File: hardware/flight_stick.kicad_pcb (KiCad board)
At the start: 4 copper layers, 76 x 51.5 mm, 60 parts, among them J1 Conn_01x04_Male, J10 USB_C_Receptacle_USB2.0, J12 Load Cell 2, J2 Conn_02x05_Odd_Even, J3 Conn_01x04_Male, J4 Load Cell 3, J6 Load Cell 1, J9 Conn_ST_STDC14, SW1 KMR223G LFG, U1 TPS62175DQC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

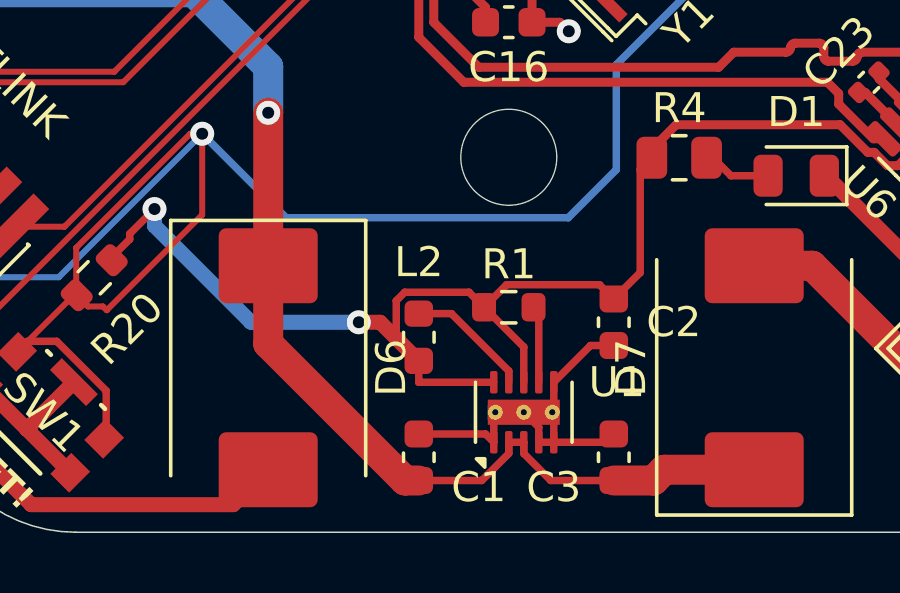
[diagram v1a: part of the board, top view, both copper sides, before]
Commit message: tied PG to mcu reset
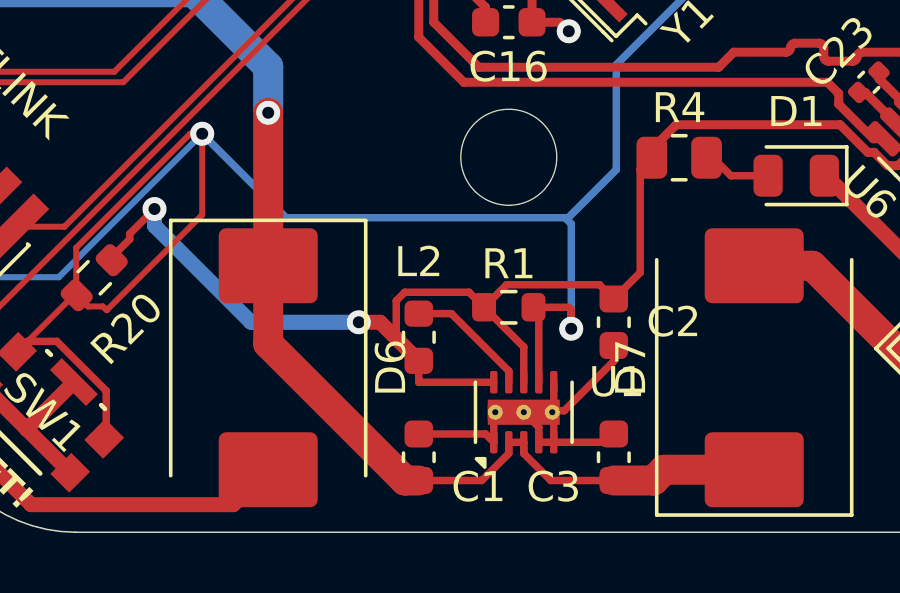
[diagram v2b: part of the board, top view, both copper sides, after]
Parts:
- R1: value 100k -> 10k
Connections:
- R1 pad 2: /Power/PG -> /RESET
- U1 pad 7: /Power/PG -> /RESET
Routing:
- net /RESET: track 64.8 -> 72.9 mm, vias 3 -> 4
- net /Power/PG: track 2.32 -> 0.00 mm
- net GND: track 155.9 -> 156.6 mm

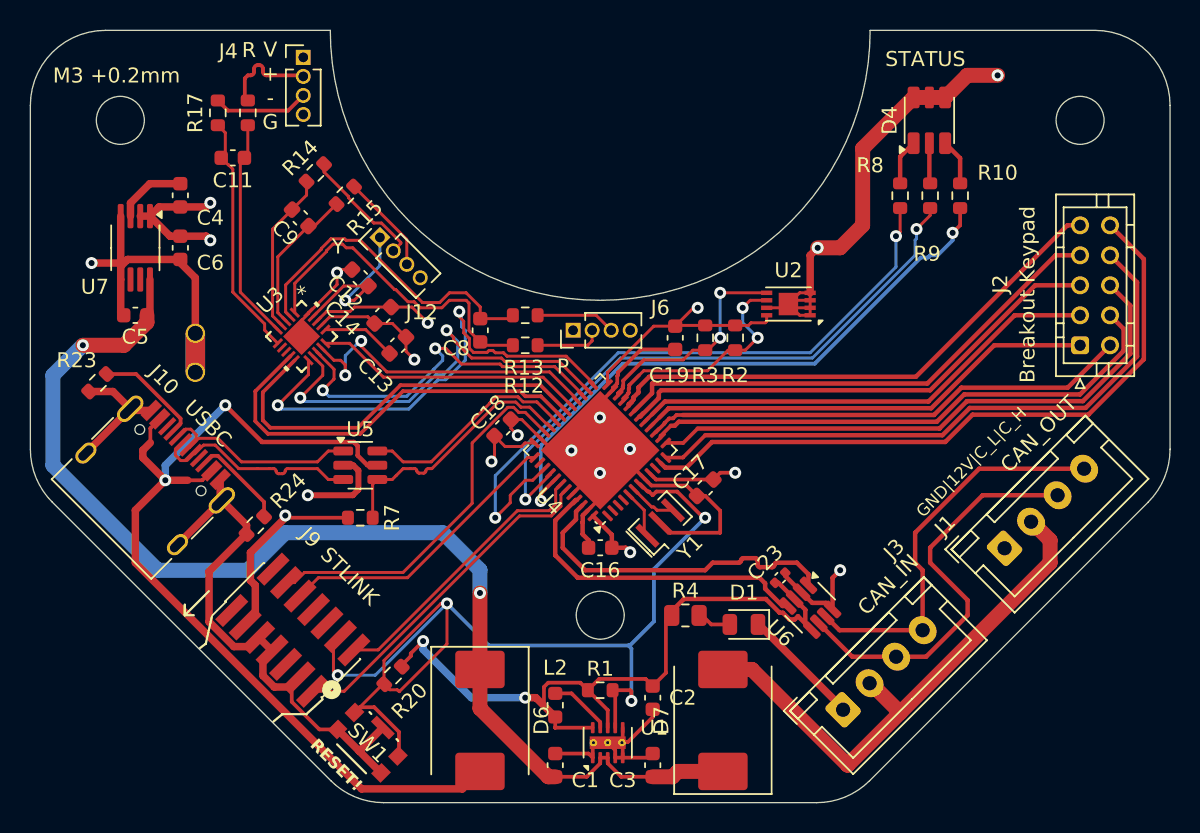
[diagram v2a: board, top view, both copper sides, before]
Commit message: clean up traces
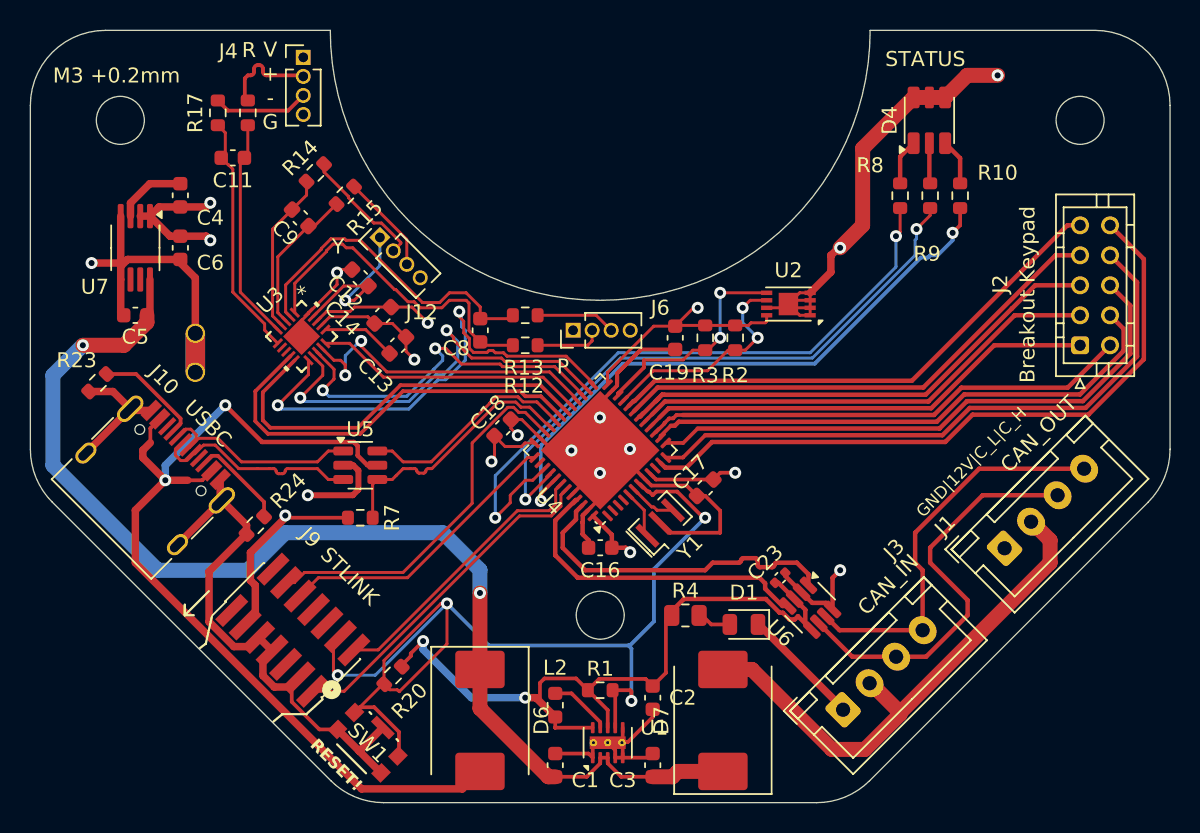
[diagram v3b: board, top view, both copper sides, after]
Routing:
- net GND: track 156.6 -> 158.5 mm
- net +12V: track 36.0 -> 35.2 mm
- net +3.3V: track 100.7 -> 101.4 mm

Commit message: Refactor netlist and lock footprints in PCB design
Renamed the /RESET net to /~{RESET} and updated all references accordingly. Reordered and renumbered net definitions to maintain consistency. Added the 'locked' attribute to multiple footprints for improved layout stability. Updated silkscreen reference positions for R8 and R10. No functional changes to the schematic or board layout.
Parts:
- removed R1: 10k, Resistor_SMD:R_0603_1608Metric
- added JP1: SolderJumper, Jumper:SolderJumper-2_P1.3mm_Open_TrianglePad1.0x1.5mm, B.Cu at (68.3, 77.6)
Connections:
- J9 pad 12: /RESET -> /~{RESET}
- R20 pad 2: /RESET -> /~{RESET}
- SW1 pad 1: /RESET -> /~{RESET}
- SW1 pad 2: /RESET -> /~{RESET}
- U1 pad 7: /RESET -> Net-(JP1-B)
- U4 pad 7: /RESET -> /~{RESET}
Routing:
- net /RESET: track 72.9 -> 0.00 mm, vias 4 -> 0
- net /~{RESET}: track 0.00 -> 46.2 mm, vias 0 -> 4
- net Net-(JP1-B): track 0.00 -> 10.5 mm, vias 0 -> 1
- net GND: track 158.5 -> 150.7 mm
- net +3.3V: track 101.4 -> 103.7 mm
- net /CAN_TX: track 22.4 -> 21.6 mm
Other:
- board text added: "Aryan Ghosh Flight Stick Rev ${REVISION}"
- board text added: "M3"
- board text added: "MCU_RST->PG"
- board text removed: "Aryan Ghosh Flight Stick Rev 5"
- board text removed: "M3 +0.2mm"

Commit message: changed to in-stock buck regulator
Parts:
- removed U1: TPS62175DQC, Package_SON:WSON-10-1EP_2x3mm_P0.5mm_EP0.84x2.4mm_ThermalVias
- added U8: TPS62177DQC, Package_SON:WSON-10-1EP_2x3mm_P0.5mm_EP0.84x2.4mm_ThermalVias, F.Cu at (74.3, 85.9)
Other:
- board text added: "ADC"
- board text added: "μC"
